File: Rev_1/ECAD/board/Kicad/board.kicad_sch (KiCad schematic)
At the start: 0 parts

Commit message: test
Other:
- added sheet MCU (mcu.kicad_sch)
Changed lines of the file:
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@@
 (kicad_sch (version 20230121) (generator eeschema)
   (paper "A4")
+  (sheet (at 26.67 74.295) (size 46.355 49.53) (fields_autoplaced)
+    (stroke (width 0.1524) (type solid))
+    (fill (color 0 0 0 0.0000))
+    (property "Sheetname" "MCU" (at 26.67 73.5834 0)
+      (effects (font (size 1.27 1.27)) (justify left bottom))
+    )
+    (property "Sheetfile" "mcu.kicad_sch" (at 26.67 124.4096 0)
+      (effects (font (size 1.27 1.27)) (justify left top))
+    )
+    (instances
+      (project "board"
+        (path "/2f4d49fd-9c63-4eb5-a266-4b5553b3e489" (page "2"))
+      )
+    )
+  )
   (sheet_instances
     (path "/" (page "1"))

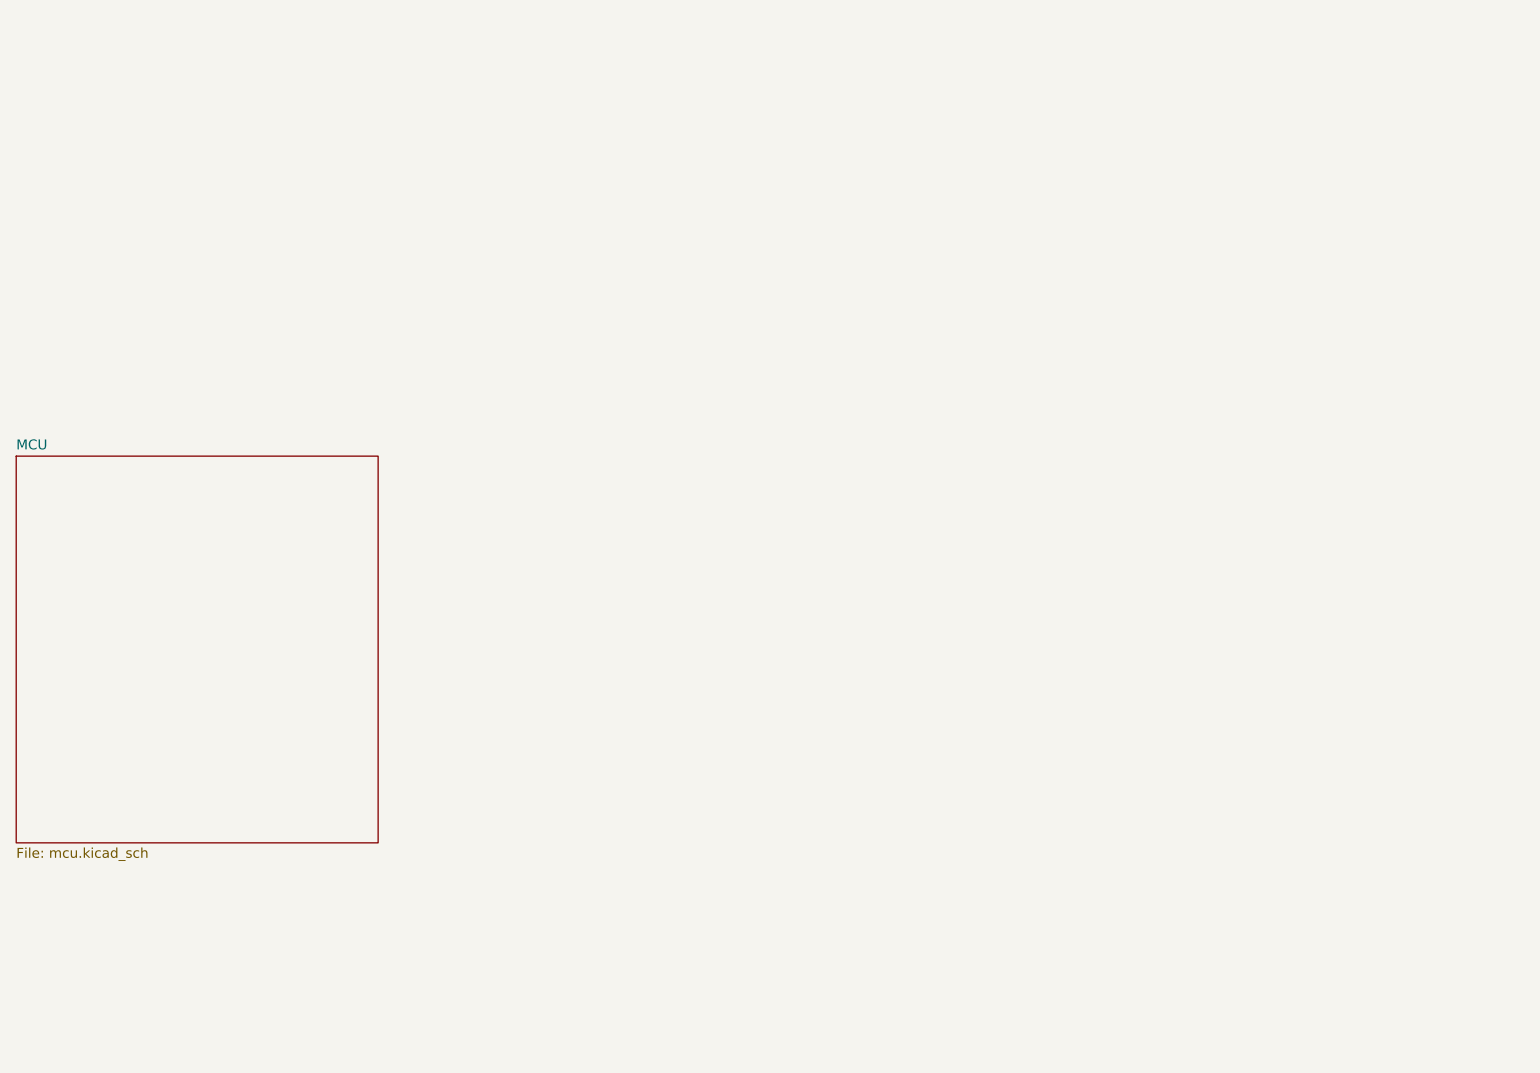
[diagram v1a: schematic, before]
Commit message: Added USB Power circiut
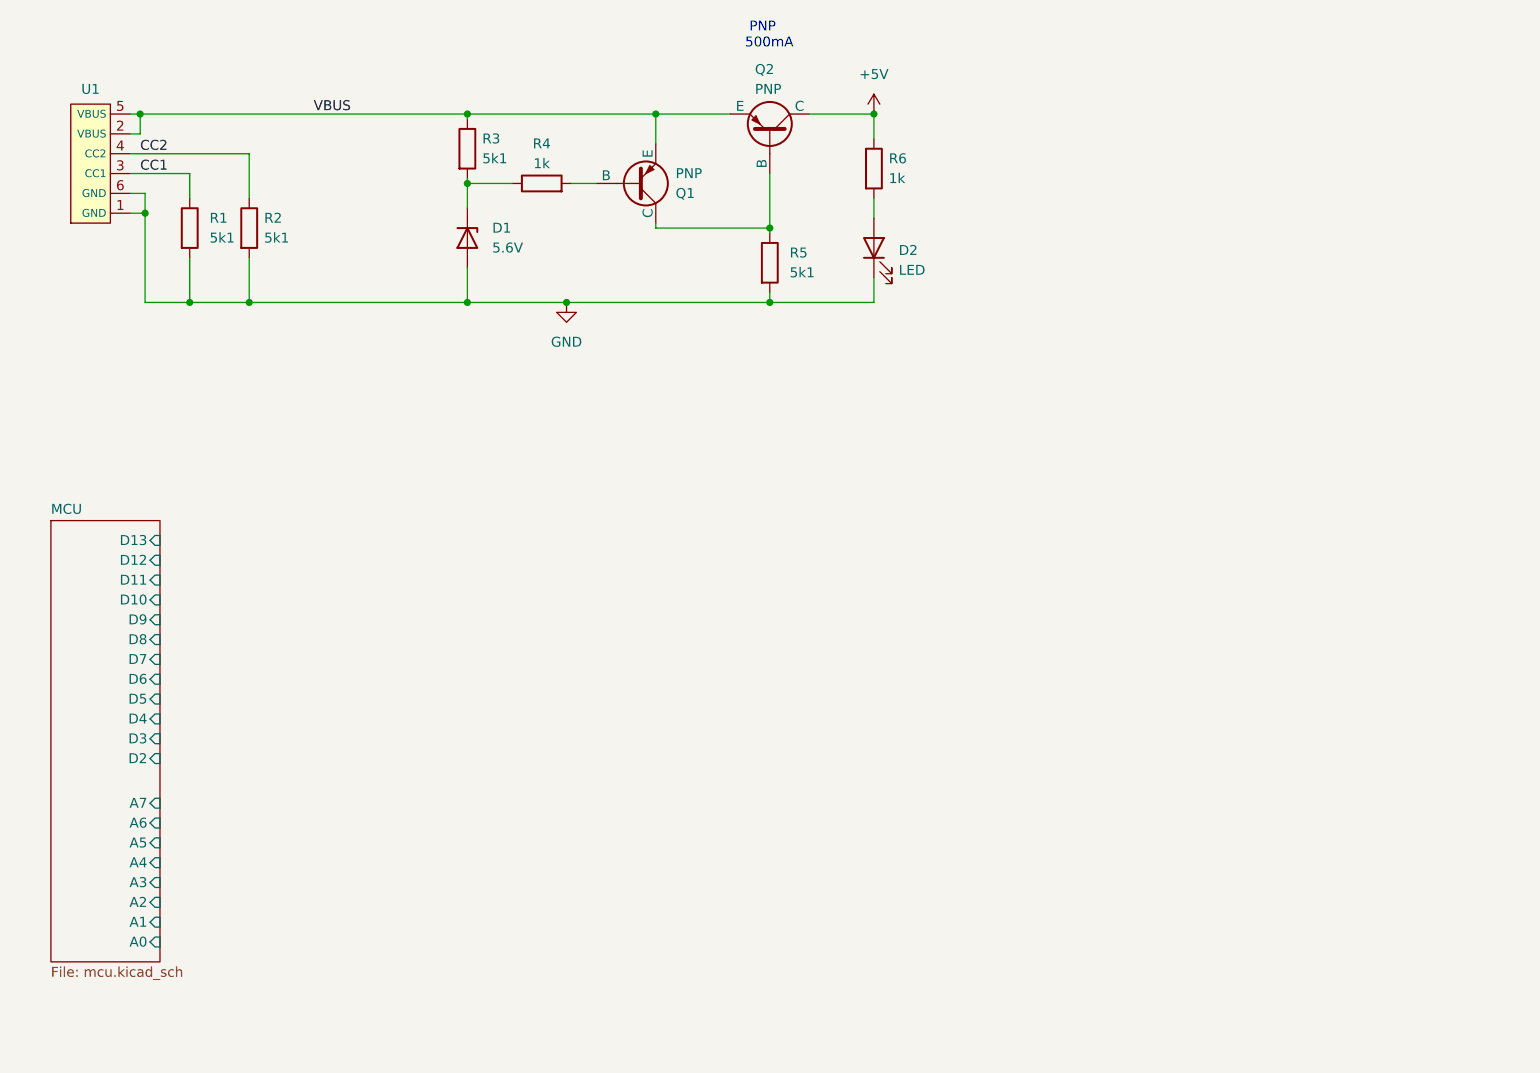
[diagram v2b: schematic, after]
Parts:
- added D1: 5.6V, Package_TO_SOT_SMD:SOT-23, symbol Device:D_Zener
- added D2: LED, symbol Device:LED
- added Q1: PNP, Package_TO_SOT_SMD:SOT-23, symbol Simulation_SPICE:PNP
- added Q2: PNP, Package_TO_SOT_THT:TO-92, symbol Simulation_SPICE:PNP
- added R1, R2, R3, R5: 5k1, Resistor_SMD:R_0805_2012Metric_Pad1.20x1.40mm_HandSolder, symbol Device:R
- added R4, R6: 1k, Resistor_SMD:R_0805_2012Metric_Pad1.20x1.40mm_HandSolder, symbol Device:R
- added U1: ~, symbol EEPROM_PROGRAMMER:USB_C_6PIN
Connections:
- new net: Q1.1 (C), Q2.2 (B), R5.1
- new net: Q1.2 (B), R4.2
- new net: D1.1 (K), R3.2, R4.1
- new net: D2.2 (A), R6.2
- new net +5V: Q2.1 (C), R6.1
- new net CC1: R1.1, U1.3 (CC1)
- new net CC2: R2.1, U1.4 (CC2)
- new net GND: D1.2 (A), D2.1 (K), R1.2, R2.2, R5.2, U1.1 (GND), U1.6 (GND)
- new net VBUS: Q1.3 (E), Q2.3 (E), R3.1, U1.2 (VBUS), U1.5 (VBUS)
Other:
- sheet MCU ports: added A0, A1, A2, A3, A4, A5, A6, A7, D10, D11, D12, D13, D2, D3, D4, D5, D6, D7, D8, D9; removed none
- note added: "PNP 500mA"

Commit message: Added power unit, and started on the logic block
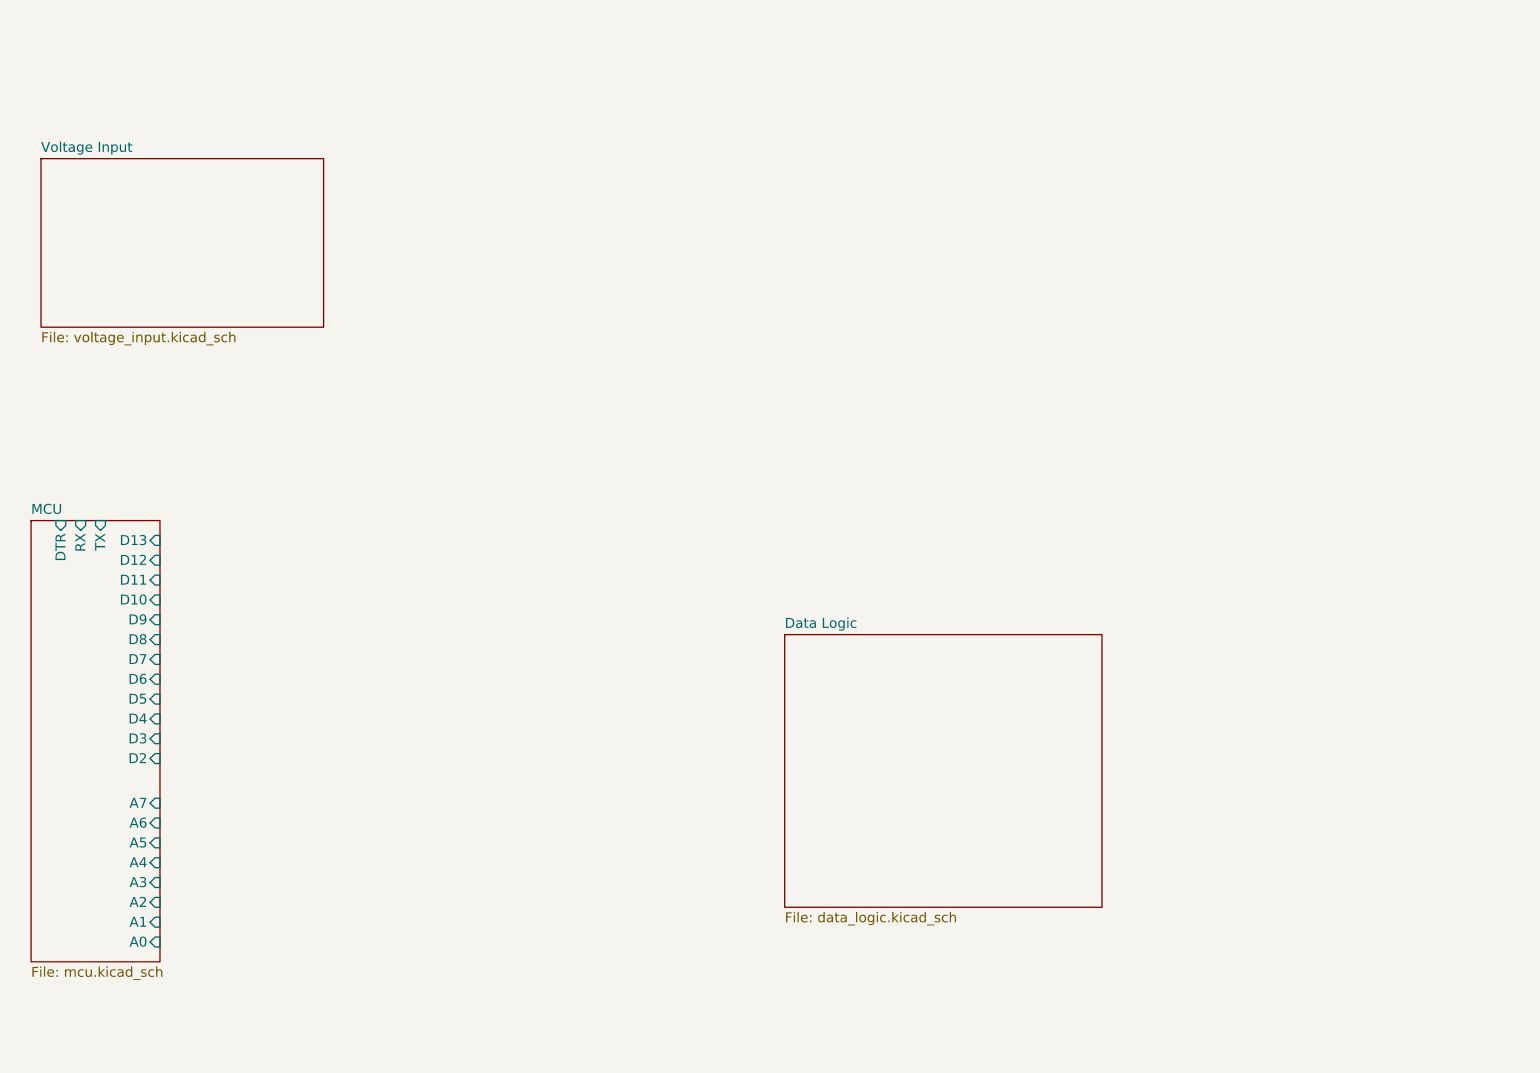
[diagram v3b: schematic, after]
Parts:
- removed D1: 5.6V, Package_TO_SOT_SMD:SOT-23, symbol Device:D_Zener
- removed D2: LED, symbol Device:LED
- removed Q1: PNP, Package_TO_SOT_SMD:SOT-23, symbol Simulation_SPICE:PNP
- removed Q2: PNP, Package_TO_SOT_THT:TO-92, symbol Simulation_SPICE:PNP
- removed R1, R2, R3, R5: 5k1, Resistor_SMD:R_0805_2012Metric_Pad1.20x1.40mm_HandSolder, symbol Device:R
- removed R4, R6: 1k, Resistor_SMD:R_0805_2012Metric_Pad1.20x1.40mm_HandSolder, symbol Device:R
- removed U1: ~, symbol EEPROM_PROGRAMMER:USB_C_6PIN
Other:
- added sheet Data Logic (data_logic.kicad_sch)
- added sheet Voltage Input (voltage_input.kicad_sch)
- sheet MCU ports: added DTR, RX, TX; removed none
- note removed: "PNP 500mA"
- title: (none) -> EEPROM Programer

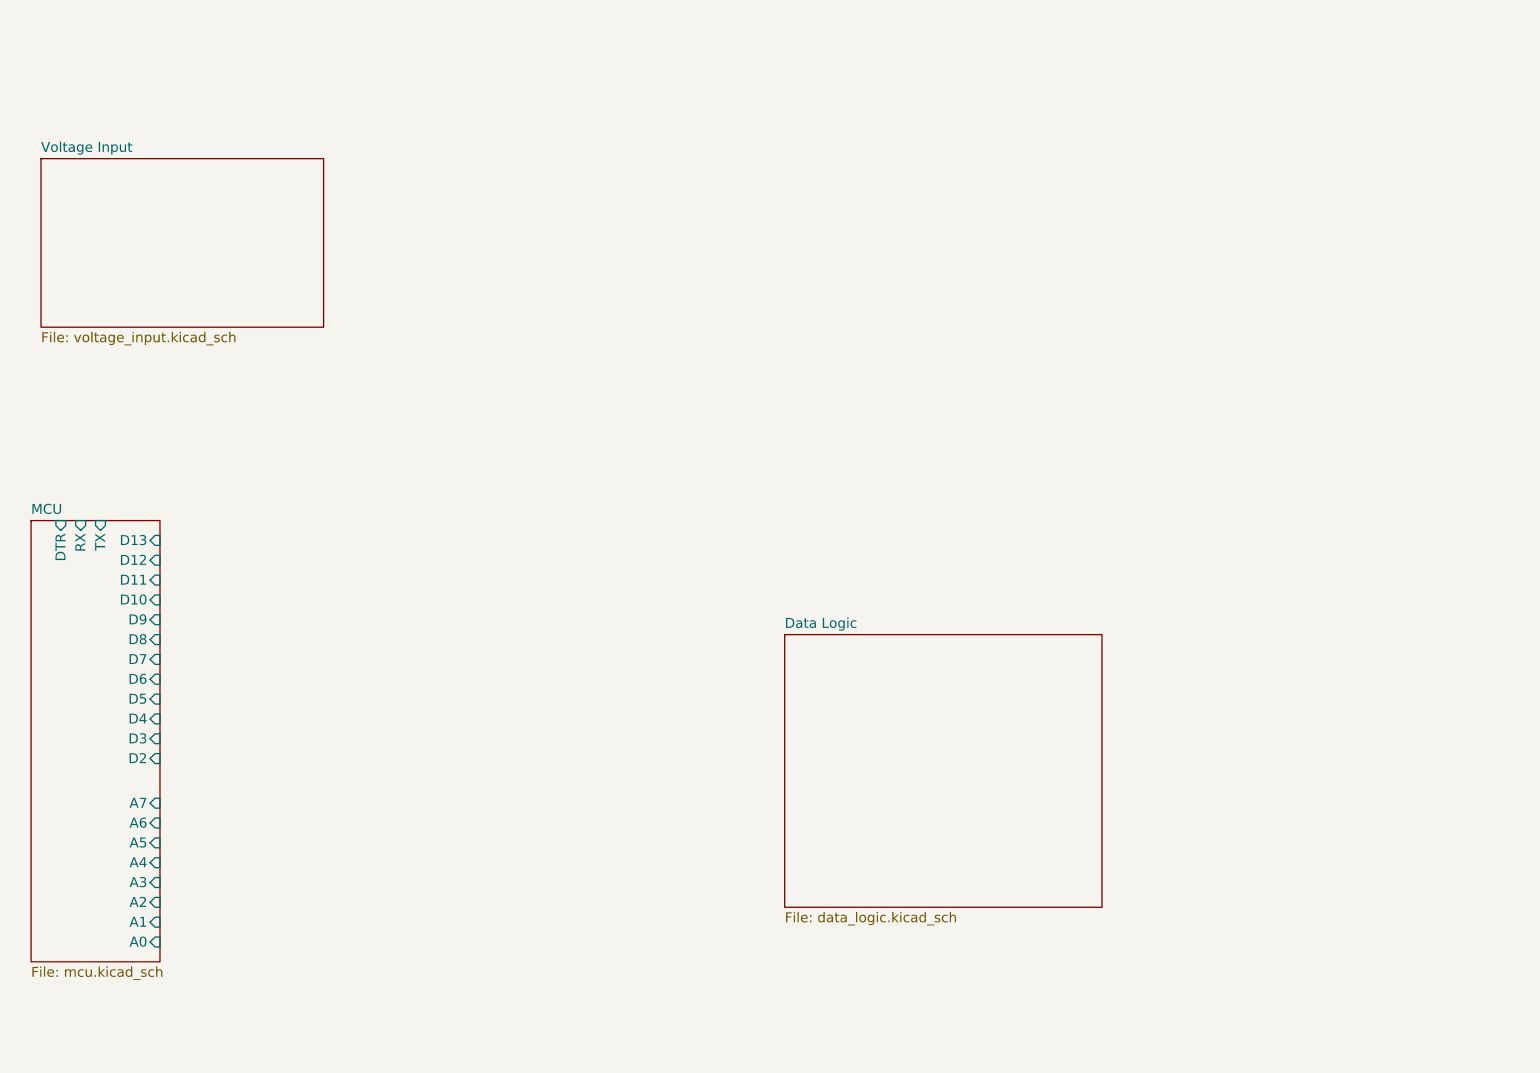
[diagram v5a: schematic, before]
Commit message: Updated Symbol library´and added SD Card Reader to schematic
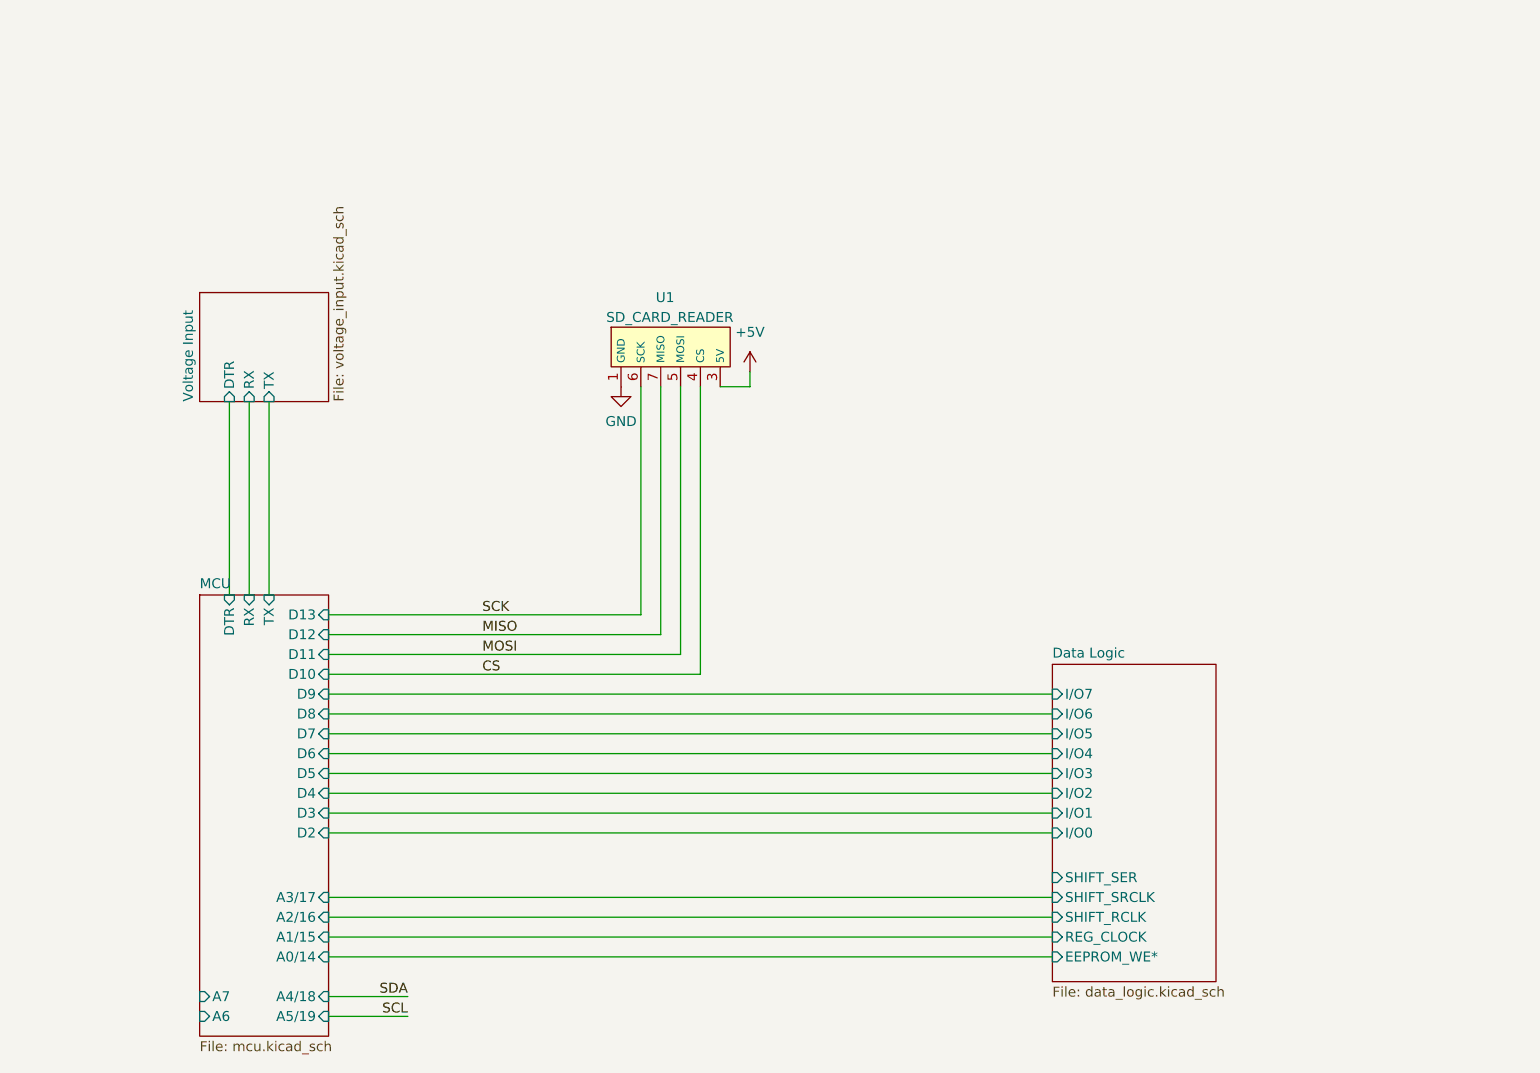
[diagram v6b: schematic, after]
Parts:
- added U1: SD_CARD_READER, symbol EEPROM_PROGRAMMER:SD_CARD_READER
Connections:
- new net +5V: U1.3 (5V)
- new net CS: U1.4 (CS)
- new net GND: U1.1 (GND)
- new net MISO: U1.7 (MISO)
- new net MOSI: U1.5 (MOSI)
- new net SCK: U1.6 (SCK)
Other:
- sheet Data Logic ports: added EEPROM_WE*, I/O0, I/O1, I/O2, I/O3, I/O4, I/O5, I/O6, I/O7, REG_CLOCK, SHIFT_RCLK, SHIFT_SER, SHIFT_SRCLK; removed none
- sheet MCU ports: added A0/14, A1/15, A2/16, A3/17, A4/18, A5/19; removed A0, A1, A2, A3, A4, A5
- sheet Voltage Input ports: added DTR, RX, TX; removed none
